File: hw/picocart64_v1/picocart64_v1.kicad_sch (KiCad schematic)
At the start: 13 parts, among them J1 USB_C_Receptacle_USB2.0, J2 Conn_ARM_JTAG_SWD_10, Q1 BSS84, SW1 BootButton, U1 LY68L6400SLIT, U2 LY68L6400SLIT, U3 RP2040_Stamp, U4 N64-Cartridge

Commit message: Everything routed
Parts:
- removed J2: Conn_ARM_JTAG_SWD_10, symbol Connector:Conn_ARM_JTAG_SWD_10
- added C1, C2: 100n, Capacitor_SMD:C_0603_1608Metric, symbol Device:C_Small
- added J2: Conn_01x05, Connector_PinHeader_2.54mm:PinHeader_1x05_P2.54mm_Vertical, symbol Connector_Generic:Conn_01x05
- added JP1, JP2, JP3, JP4: SolderJumper_2_Open, Jumper:SolderJumper-2_P1.3mm_Open_TrianglePad1.0x1.5mm, symbol Jumper:SolderJumper_2_Open
- J1: footprint (none) -> Connector_USB_Extra:USB_C_Receptacle_GT-USB-7010
- SW1: footprint (none) -> Button_Switch_SMD:SW_SPST_FSMSM
- U4: footprint (none) -> picocart64:N64-Connector
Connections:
- net +3V3: now also C1.1, C2.1, J2.1 (Pin_1)
- net GND: now also C1.2, C2.2, J2.5 (Pin_5)
- net N64_EEP_SDAT: now also JP3.2 (B)
- net N64_NMI: now also JP4.2 (B)
- net N64_SI_CLK: now also JP2.2 (B)
- net N64_S_DAT: now also JP1.2 (B)
- net QSPI_RAM_CS0: now also JP1.1 (A)
- net QSPI_RAM_CS1: now also JP2.1 (A)
- net QSPI_RAM_IO0: now also JP4.1 (A)
- net QSPI_RAM_SCK: now also JP3.1 (A)
- net RP_SWDCLK: now also J2.3 (Pin_3)
- net RP_SWDIO: now also J2.4 (Pin_4)
- net ~{RP_RESET}: now also J2.2 (Pin_2)
- net VBUS_unf: now reaches FB1.1, J1.A4 (VBUS), J1.A9 (VBUS), J1.B4 (VBUS), J1.B9 (VBUS)
- no-connect marks 17 -> 11
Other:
- moved on the sheet: FB1

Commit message: hw: checkpoint
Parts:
- removed C1, C2: 100n, Capacitor_SMD:C_0603_1608Metric, symbol Device:C_Small
- removed R4: 10k, Resistor_SMD:R_0603_1608Metric, symbol Device:R_Small
- removed U1, U2: LY68L6400SLIT, Package_SO:SOIC-8_5.275x5.275mm_P1.27mm, symbol spiram:LY68L6400SLIT
- added J3: Conn_02x06_Odd_Even, Connector_PinSocket_2.54mm:PinSocket_2x06_P2.54mm_Horizontal, symbol Connector_Generic:Conn_02x06_Odd_Even
- added J4: Micro_SD_Card_Det, Connector_Card:microSD_HC_Molex_104031-0811, symbol Connector:Micro_SD_Card_Det
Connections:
- net +3V3: now also J3.1 (Pin_1), J3.2 (Pin_2), J4.4 (VDD)
- net GND: now also J3.3 (Pin_3), J3.4 (Pin_4), J4.11 (SHIELD), J4.6 (VSS), J4.9 (DET_B)
- net QSPI_RAM_CS0 renamed PMOD_5_SIO2
- net PMOD_5_SIO2: now also J3.12 (Pin_12), J4.1 (DAT2)
- net QSPI_RAM_CS1 renamed PMOD_6_SIO3
- net PMOD_6_SIO3: now also J3.10 (Pin_10), J4.2 (DAT3/CD)
- net QSPI_RAM_IO0 renamed PMOD_4_SCLK
- net PMOD_4_SCLK: now also J3.5 (Pin_5), J4.5 (CLK)
- net QSPI_RAM_IO1 renamed PMOD_2_SIO0
- net PMOD_2_SIO0: now also J3.9 (Pin_9), J4.7 (DAT0)
- net QSPI_RAM_IO2 renamed PMOD_3_SIO1
- net PMOD_3_SIO1: now also J3.7 (Pin_7), J4.8 (DAT1)
- net QSPI_RAM_IO3 renamed PMOD_7_CS0
- net PMOD_7_CS0: now also J3.8 (Pin_8), J4.10 (DET_A)
- net QSPI_RAM_SCK renamed PMOD_1_SS
- net PMOD_1_SS: now also J3.11 (Pin_11), J4.3 (CMD)
- new net PMOD_8_CS1: J3.6 (Pin_6)
- no-connect marks 11 -> 12
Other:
- moved on the sheet: Q1

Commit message: hw: PicoCart64 V1.0
First exploratory revision
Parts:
- U3: footprint RP2040_Stamp:RP2040_Stamp_SMD -> RP2040_Stamp:RP2040_Stamp_FlexyPin
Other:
- company: (none) -> Konrad Beckmann
- title: (none) -> PicoCart64
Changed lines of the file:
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@@
 (kicad_sch (version 20211123) (generator eeschema)
   (paper "A4")
+  (title_block
+    (title "PicoCart64")
+    (date "2022-06-22")
+    (rev "V1.0")
+    (company "Konrad Beckmann")
+  )
   (junction (at 45.72 45.72) (diameter 0) (color 0 0 0 0)
   )
@@
     (property "Reference" "U3" (id 0) (at 119.38 17.78 0))
     (property "Value" "RP2040_Stamp" (id 1) (at 119.38 20.32 0))
-    (property "Footprint" "RP2040_Stamp:RP2040_Stamp_SMD" (id 2) (at 119.38 105.41 0)
+    (property "Footprint" "RP2040_Stamp:RP2040_Stamp_FlexyPin" (id 2) (at 119.38 105.41 0)
       (effects (font (size 1.27 1.27)) hide)
     )
@@
     )
     (path "/a0fcb198-ccb6-40d8-be65-0bf4fbd463d8"
-      (reference "U3") (unit 1) (value "RP2040_Stamp") (footprint "RP2040_Stamp:RP2040_Stamp_SMD")
+      (reference "U3") (unit 1) (value "RP2040_Stamp") (footprint "RP2040_Stamp:RP2040_Stamp_FlexyPin")
     )
     (path "/69e1df44-123d-446b-8e62-8562dbf7e39b"

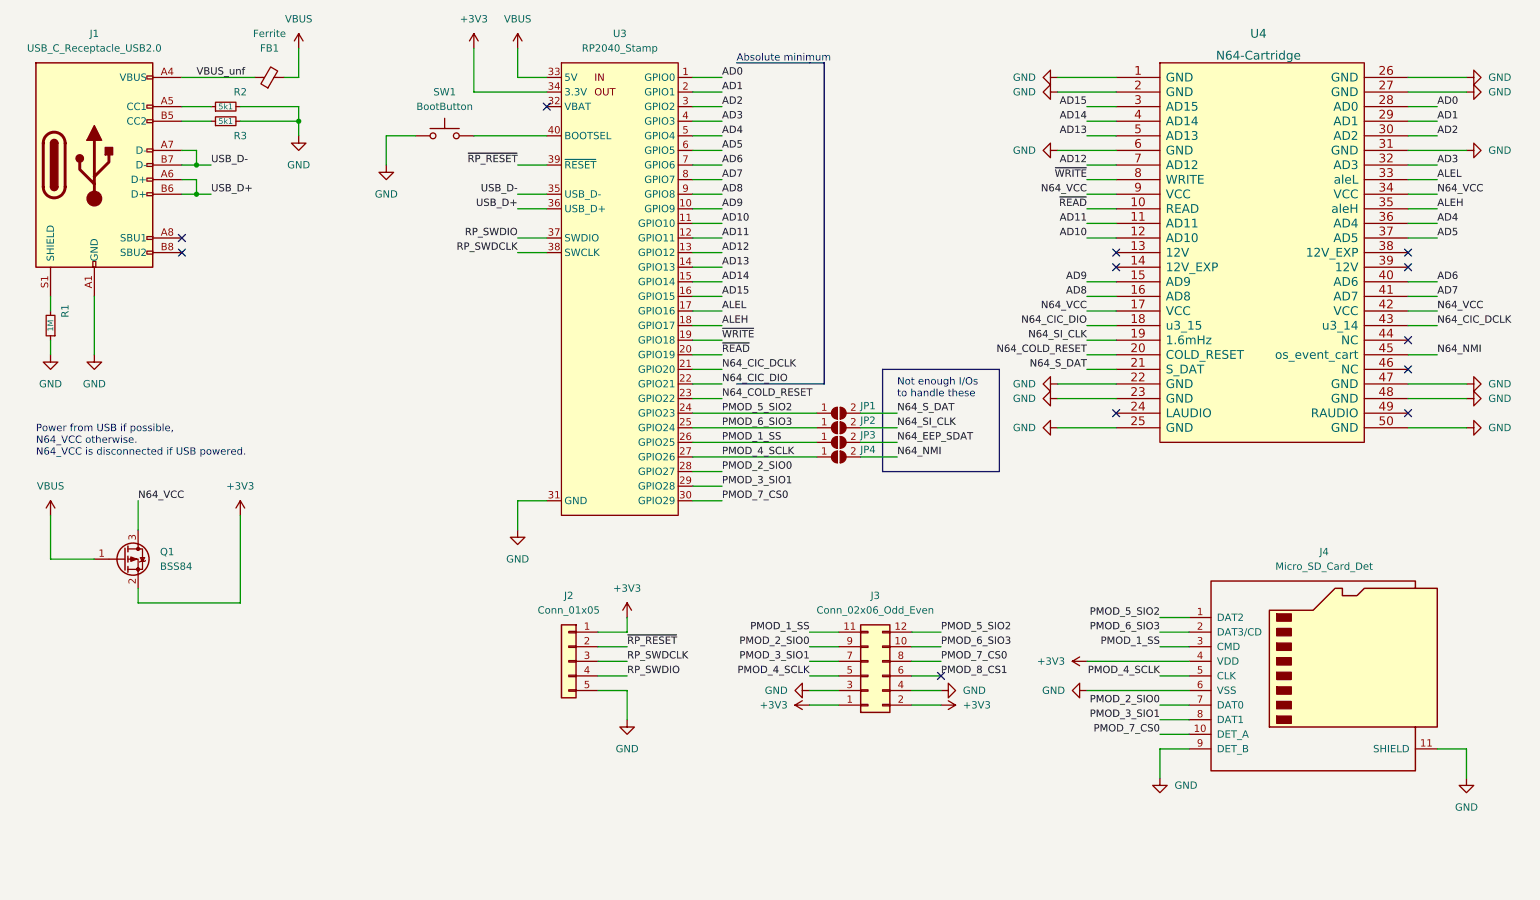
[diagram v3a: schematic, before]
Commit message: hw: Add concept drawing of PicoCart v2.0
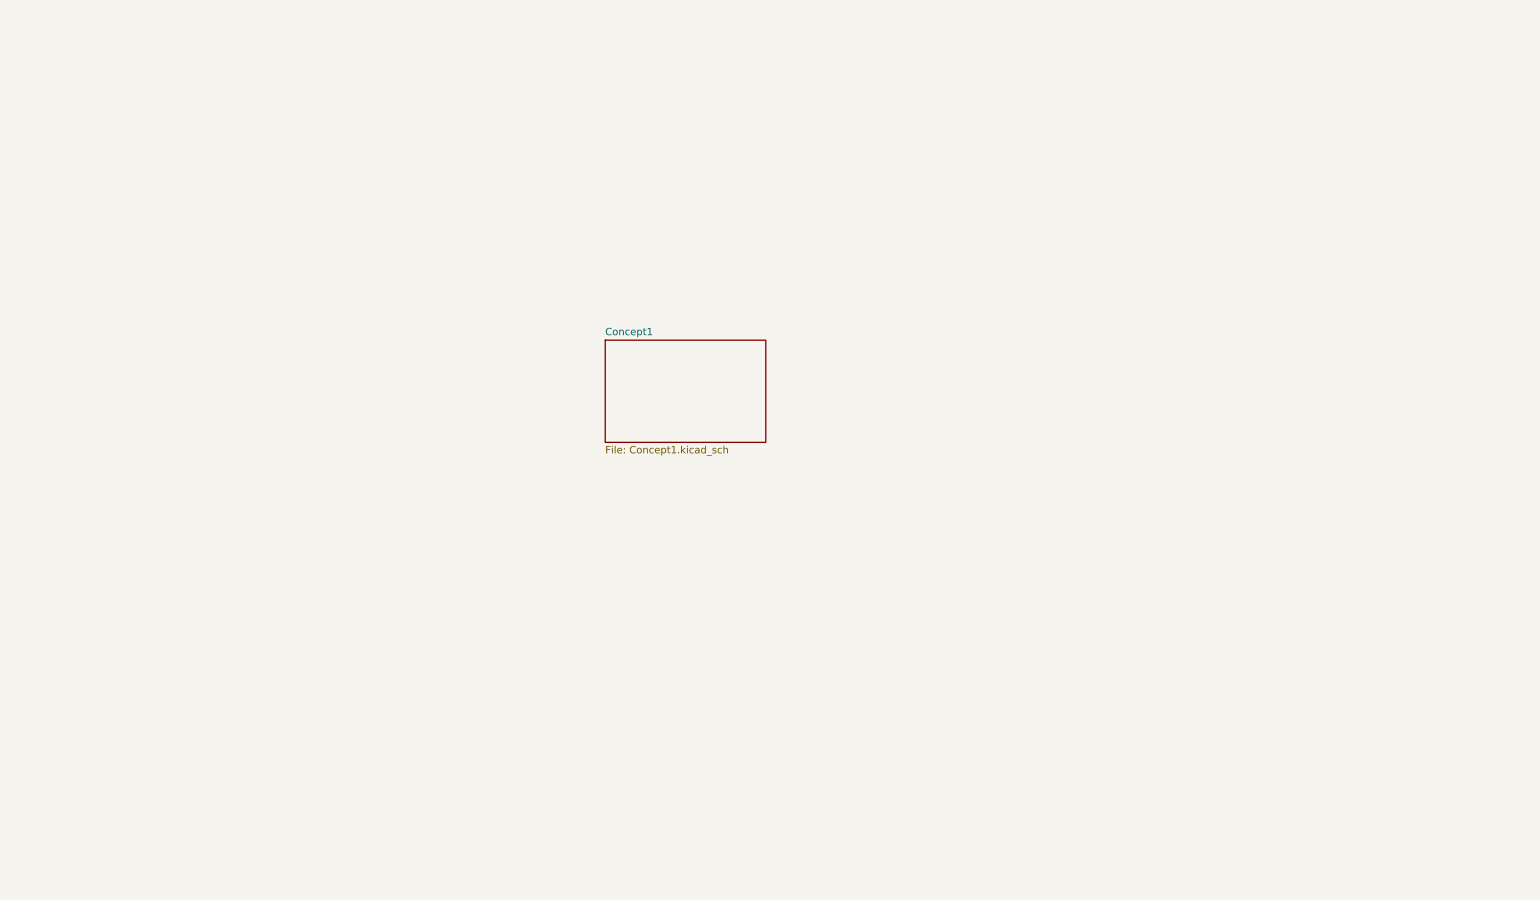
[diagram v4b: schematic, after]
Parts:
- removed FB1: Ferrite, Inductor_SMD:L_0603_1608Metric, symbol Device:FerriteBead_Small
- removed J1: USB_C_Receptacle_USB2.0, Connector_USB_Extra:USB_C_Receptacle_GT-USB-7010, symbol Connector:USB_C_Receptacle_USB2.0
- removed J2: Conn_01x05, Connector_PinHeader_2.54mm:PinHeader_1x05_P2.54mm_Vertical, symbol Connector_Generic:Conn_01x05
- removed J3: Conn_02x06_Odd_Even, Connector_PinSocket_2.54mm:PinSocket_2x06_P2.54mm_Horizontal, symbol Connector_Generic:Conn_02x06_Odd_Even
- removed J4: Micro_SD_Card_Det, Connector_Card:microSD_HC_Molex_104031-0811, symbol Connector:Micro_SD_Card_Det
- removed JP1, JP2, JP3, JP4: SolderJumper_2_Open, Jumper:SolderJumper-2_P1.3mm_Open_TrianglePad1.0x1.5mm, symbol Jumper:SolderJumper_2_Open
- removed Q1: BSS84, Package_TO_SOT_SMD:SOT-23, symbol Transistor_FET:BSS84
- removed R1: 1M, Resistor_SMD:R_0603_1608Metric, symbol Device:R_Small
- removed R2, R3: 5k1, Resistor_SMD:R_0603_1608Metric, symbol Device:R_Small
- removed SW1: BootButton, Button_Switch_SMD:SW_SPST_FSMSM, symbol Switch:SW_Push
- removed U3: RP2040_Stamp, RP2040_Stamp:RP2040_Stamp_FlexyPin, symbol RP2040_Stamp:RP2040_Stamp
- removed U4: N64-Cartridge, picocart64:N64-Connector, symbol n64-cartridge:N64-Cartridge
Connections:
- no-connect marks 12 -> 0
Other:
- added sheet Concept1 (Concept1.kicad_sch)
- note removed: "Absolute minimum"
- note removed: "Not enough I/Os to handle these"
- note removed: "Power from USB if possible, N64_VCC otherwise. N64_VCC is disconnected if USB powered."

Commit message: hw: Concept2, is this the future?
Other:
- added sheet Concept2 (Concept2.kicad_sch)

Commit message: hw: Concept3
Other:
- added sheet Concept3 (Concept3.kicad_sch)
